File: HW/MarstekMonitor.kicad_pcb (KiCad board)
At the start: 2 copper layers, 70 x 33.5 mm, 10 parts, among them J1 Conn_01x06_Socket

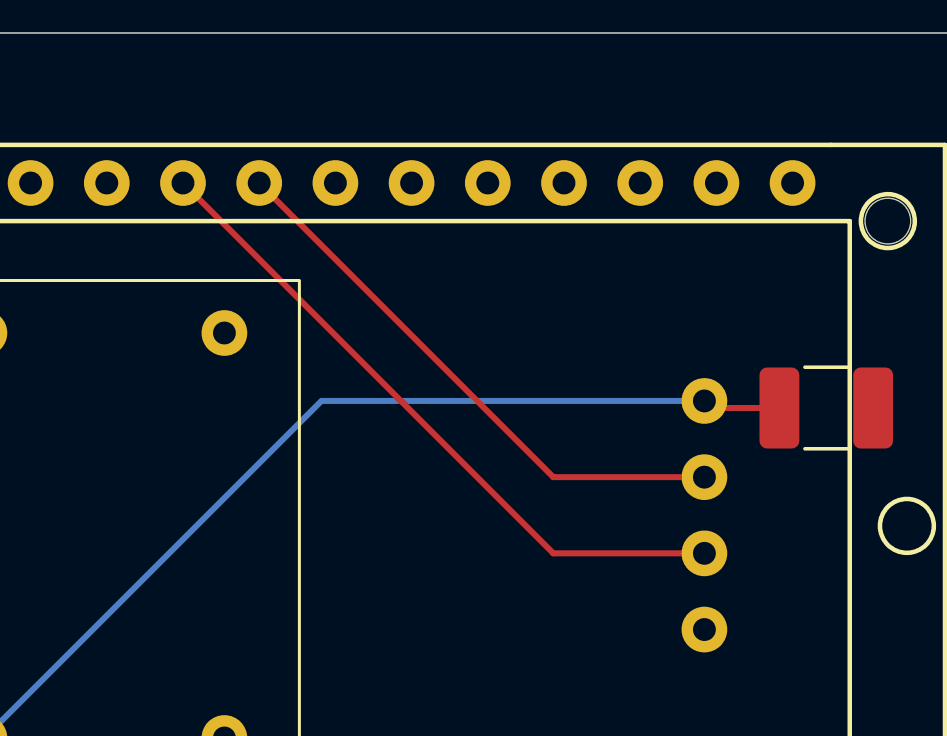
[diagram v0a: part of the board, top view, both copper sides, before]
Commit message: PCB layout updated
Fixed wrong GPIO pin for RX
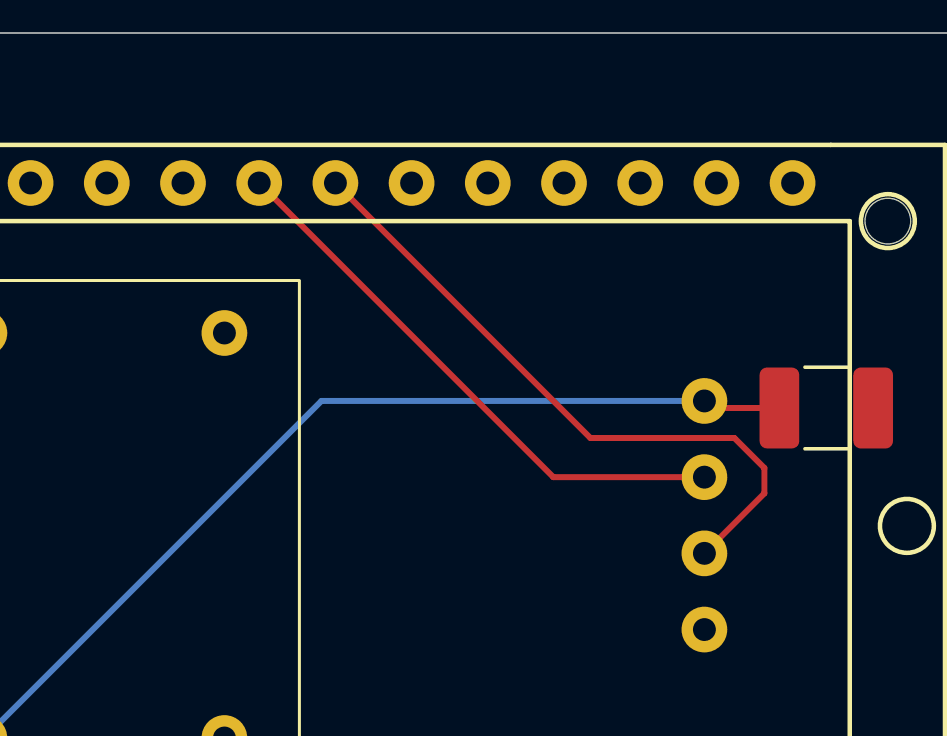
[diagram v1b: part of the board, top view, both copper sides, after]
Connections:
- TTGO1 pad 19: unconnected-(TTGO1-GPIO15-Pad19) -> /RXD
- TTGO1 pad 21: /RXD -> unconnected-(TTGO1-GPIO12-Pad21)
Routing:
- net /RXD: track 22.5 -> 21.9 mm
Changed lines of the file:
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@@
 			(psa4output no)
 			(plot_black_and_white yes)
-			(plotinvisibletext no)
 			(sketchpadsonfab no)
 			(plotpadnumbers no)
@@
 	(net 12 "unconnected-(TTGO1-SVP-Pad11)")
 	(net 13 "unconnected-(TTGO1-GPIO38-Pad9)")
-	(net 14 "unconnected-(TTGO1-GPIO15-Pad19)")
+	(net 14 "unconnected-(TTGO1-GPIO12-Pad21)")
 	(net 15 "unconnected-(TTGO1-3.3V-Pad24)")
 	(net 16 "/RXD")
@@
 			(layers "*.Cu" "*.Mask")
 			(remove_unused_layers no)
-			(net 14 "unconnected-(TTGO1-GPIO15-Pad19)")
+			(net 16 "/RXD")
 			(pinfunction "GPIO15")
-			(pintype "unspecified+no_connect")
+			(pintype "unspecified")
 		)
 		(pad "20" thru_hole circle
@@
 			(layers "*.Cu" "*.Mask")
 			(remove_unused_layers no)
-			(net 16 "/RXD")
+			(net 14 "unconnected-(TTGO1-GPIO12-Pad21)")
 			(pinfunction "GPIO12")
-			(pintype "unspecified")
+			(pintype "unspecified+no_connect")
 		)
 		(pad "22" thru_hole circle
@@
 	)
 	(segment
-		(start 124.12 67.5)
-		(end 136.465 79.845)
+		(start 129.2 67.5)
+		(end 137.7 76)
 		(width 0.2)
 		(layer "F.Cu")
@@
 	)
 	(segment
-		(start 136.465 79.845)
+		(start 137.7 76)
+		(end 142.5 76)
+		(width 0.2)
+		(layer "F.Cu")
+		(net 16)
+	)
+	(segment
+		(start 142.5 76)
+		(end 143.5 77)
+		(width 0.2)
+		(layer "F.Cu")
+		(net 16)
+	)
+	(segment
+		(start 143.5 77)
+		(end 143.5 77.845)
+		(width 0.2)
+		(layer "F.Cu")
+		(net 16)
+	)
+	(segment
+		(start 143.5 77.845)
 		(end 141.5 79.845)
 		(width 0.2)
